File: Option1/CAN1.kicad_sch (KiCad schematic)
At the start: 7 parts, among them U2 TJA1051T-3

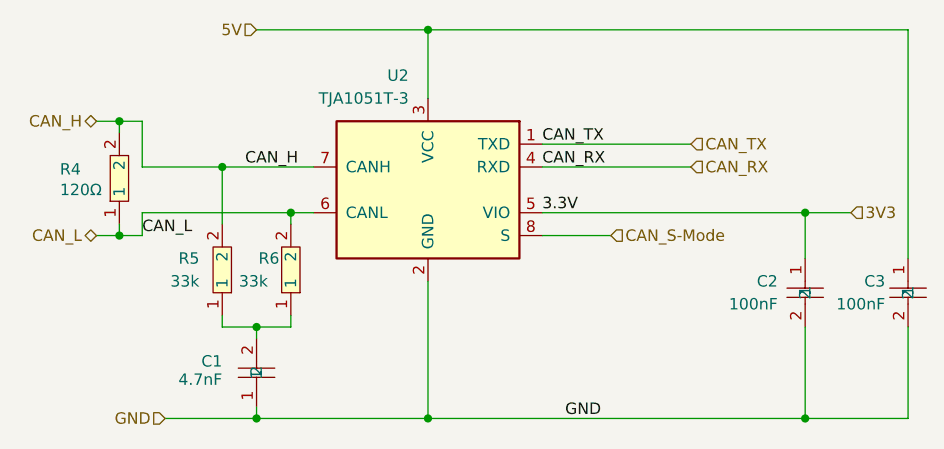
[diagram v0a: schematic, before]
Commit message: Layout für Powersupply, CAN und Stecker hinzugefügt
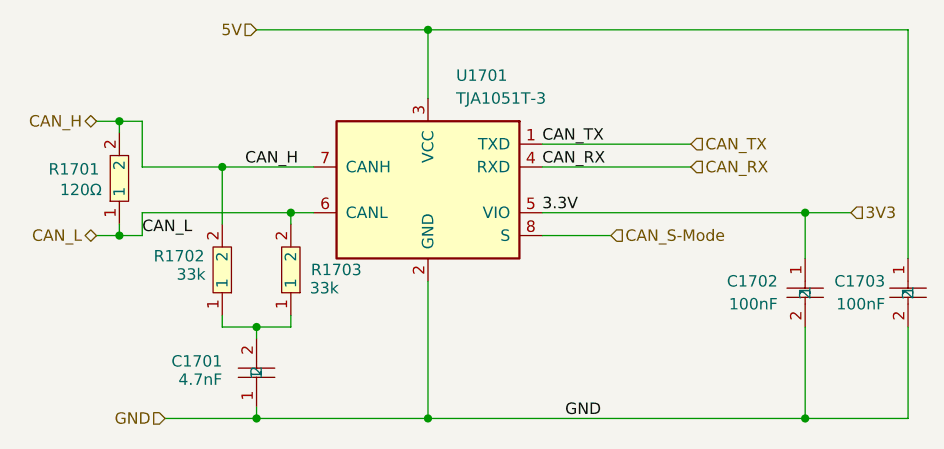
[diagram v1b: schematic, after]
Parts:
- renumbered C1 to C1701, C2 to C1702, C3 to C1703, R4 to R1701, R5 to R1702, R6 to R1703, U2 to U1701
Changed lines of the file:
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@@
 		(on_board yes)
 		(dnp no)
-		(property "Reference" "C2"
+		(property "Reference" "C1702"
 			(at 127.762 72.39 90)
 			(effects
@@
 			(project "Option1"
 				(path "/b9e5f262-9648-4b79-bdd1-af888b822329/5db2deb0-465f-47af-ae7a-0e9eee3d563c"
-					(reference "C2")
+					(reference "C1702")
 					(unit 1)
 				)
@@
 		(on_board yes)
 		(dnp no)
-		(fields_autoplaced yes)
-		(property "Reference" "R5"
-			(at 63.5 69.8499 90)
-			(effects
-				(font
-					(size 1.27 1.27)
-				)
-				(justify right)
+		(property "Reference" "R1702"
+			(at 58.42 69.596 90)
+			(effects
+				(font
+					(size 1.27 1.27)
+				)
+				(justify left)
 			)
 		)
 		(property "Value" "33k"
-			(at 63.5 72.3899 90)
-			(effects
-				(font
-					(size 1.27 1.27)
-				)
-				(justify right)
+			(at 60.96 71.628 90)
+			(effects
+				(font
+					(size 1.27 1.27)
+				)
+				(justify left)
 			)
 		)
@@
 			(project "Option1"
 				(path "/b9e5f262-9648-4b79-bdd1-af888b822329/5db2deb0-465f-47af-ae7a-0e9eee3d563c"
-					(reference "R5")
+					(reference "R1702")
 					(unit 1)
 				)
@@
 		(on_board yes)
 		(dnp no)
-		(property "Reference" "C3"
+		(property "Reference" "C1703"
 			(at 139.7 72.39 90)
 			(effects
@@
 			(project "Option1"
 				(path "/b9e5f262-9648-4b79-bdd1-af888b822329/5db2deb0-465f-47af-ae7a-0e9eee3d563c"
-					(reference "C3")
+					(reference "C1703")
 					(unit 1)
 				)
@@
 		(on_board yes)
 		(dnp no)
-		(property "Reference" "R4"
-			(at 48.006 59.944 90)
+		(property "Reference" "R1701"
+			(at 46.736 59.944 90)
 			(effects
 				(font
@@
 			(project "Option1"
 				(path "/b9e5f262-9648-4b79-bdd1-af888b822329/5db2deb0-465f-47af-ae7a-0e9eee3d563c"
-					(reference "R4")
+					(reference "R1701")
 					(unit 1)
 				)
@@
 		(dnp no)
 		(fields_autoplaced yes)
-		(property "Reference" "U2"
-			(at 86.7567 49.53 0)
-			(effects
-				(font
-					(size 1.27 1.27)
-				)
-				(justify left)
+		(property "Reference" "U1701"
+			(at 92.0181 49.53 0)
+			(effects
+				(font
+					(size 1.27 1.27)
+				)
+				(justify right)
 			)
 		)
 		(property "Value" "TJA1051T-3"
-			(at 86.7567 52.07 0)
-			(effects
-				(font
-					(size 1.27 1.27)
-				)
-				(justify left)
+			(at 92.0181 52.07 0)
+			(effects
+				(font
+					(size 1.27 1.27)
+				)
+				(justify right)
 			)
 		)
@@
 			(project "Option1"
 				(path "/b9e5f262-9648-4b79-bdd1-af888b822329/5db2deb0-465f-47af-ae7a-0e9eee3d563c"
-					(reference "U2")
+					(reference "U1701")
 					(unit 1)
 				)
@@
 		(on_board yes)
 		(dnp no)
-		(property "Reference" "C1"
+		(property "Reference" "C1701"
 			(at 66.04 81.2799 90)
 			(effects
@@
 			(project "Option1"
 				(path "/b9e5f262-9648-4b79-bdd1-af888b822329/5db2deb0-465f-47af-ae7a-0e9eee3d563c"
-					(reference "C1")
+					(reference "C1701")
 					(unit 1)
 				)
@@
 		(on_board yes)
 		(dnp no)
-		(property "Reference" "R6"
-			(at 72.39 69.85 90)
+		(property "Reference" "R1703"
+			(at 81.534 71.12 90)
 			(effects
 				(font
@@
 		)
 		(property "Value" "33k"
-			(at 71.12 72.3899 90)
+			(at 78.994 73.152 90)
 			(effects
 				(font
@@
 			(project "Option1"
 				(path "/b9e5f262-9648-4b79-bdd1-af888b822329/5db2deb0-465f-47af-ae7a-0e9eee3d563c"
-					(reference "R6")
-					(unit 1)
-				)
+					(reference "R1703")
+					(unit 1)
+				)

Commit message: GND polygon hinzugefügt, unverbundene Pads verknüpft, 0 Ohm Widerstand für Display Strohmversorgung hinzugefügt
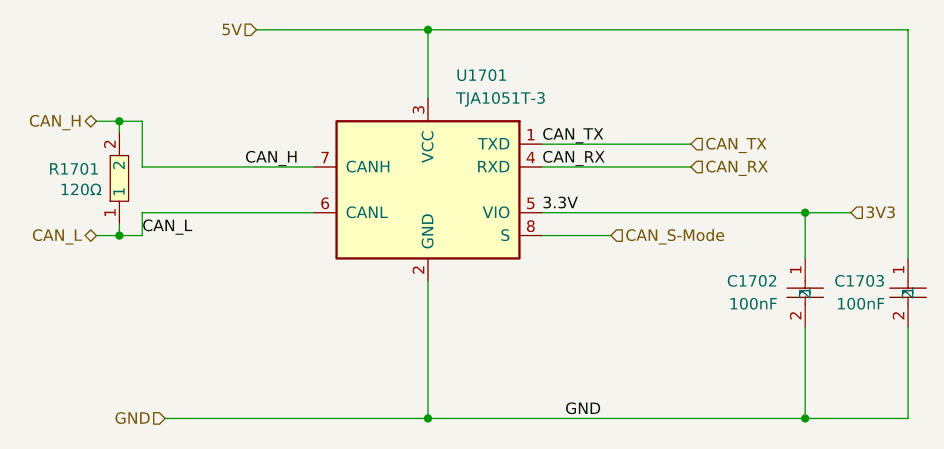
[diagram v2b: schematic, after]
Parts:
- removed C1701: 4.7nF, easyeda2kicad:C0805, symbol easyeda2kicad:0805B472K500NT
- removed R1702, R1703: 33k, easyeda2kicad:R0603, symbol easyeda2kicad:0603WAF3302T5E

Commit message: Schaltplan zu bachelorarbeit Dokument hinzuigefügt. Fertigf bis SPI Flash
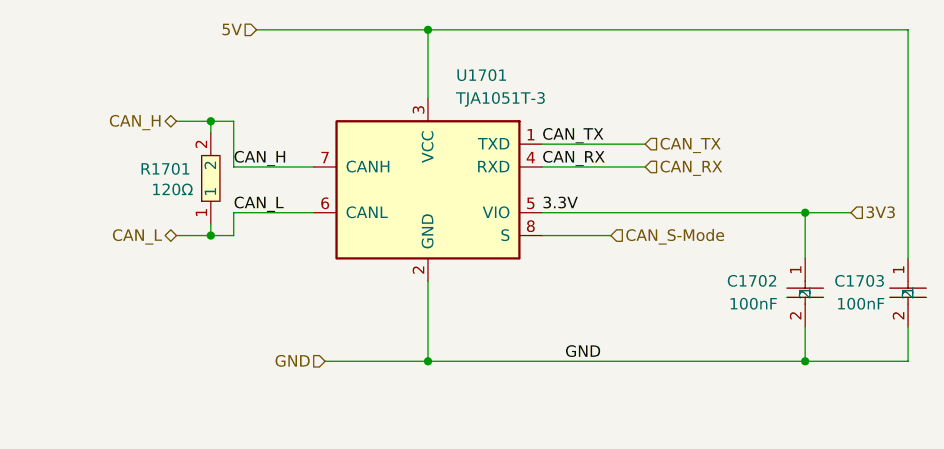
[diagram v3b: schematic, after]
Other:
- moved on the sheet: R1701
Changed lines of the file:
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@@
 	)
 	(junction
-		(at 54.61 67.31)
+		(at 130.81 81.28)
 		(diameter 0)
 		(color 0 0 0 0)
 	)
 	(junction
-		(at 54.61 54.61)
+		(at 64.77 67.31)
 		(diameter 0)
 		(color 0 0 0 0)
@@
 	)
 	(junction
-		(at 130.81 87.63)
+		(at 64.77 54.61)
+		(diameter 0)
+		(color 0 0 0 0)
+	)
+	(junction
+		(at 88.9 81.28)
 		(diameter 0)
 		(color 0 0 0 0)
@@
 		(color 0 0 0 0)
 	)
-	(junction
-		(at 88.9 87.63)
-		(diameter 0)
-		(color 0 0 0 0)
-	)
-	(wire
-		(pts
-			(xy 57.15 67.31) (xy 57.15 64.77)
+	(wire
+		(pts
+			(xy 64.77 67.31) (xy 67.31 67.31)
+		)
+		(stroke
+			(width 0)
+			(type default)
+		)
+	)
+	(wire
+		(pts
+			(xy 67.31 67.31) (xy 67.31 64.77)
 		)
 		(stroke
@@
 	(wire
 		(pts
-			(xy 142.24 87.63) (xy 130.81 87.63)
-		)
-		(stroke
-			(width 0)
-			(type default)
-		)
-	)
-	(wire
-		(pts
-			(xy 54.61 67.31) (xy 52.07 67.31)
-		)
-		(stroke
-			(width 0)
-			(type default)
-		)
-	)
-	(wire
-		(pts
-			(xy 57.15 54.61) (xy 57.15 59.69)
-		)
-		(stroke
-			(width 0)
-			(type default)
-		)
-	)
-	(wire
-		(pts
-			(xy 57.15 54.61) (xy 54.61 54.61)
-		)
-		(stroke
-			(width 0)
-			(type default)
-		)
-	)
-	(wire
-		(pts
-			(xy 57.15 64.77) (xy 76.2 64.77)
-		)
-		(stroke
-			(width 0)
-			(type default)
-		)
-	)
-	(wire
-		(pts
-			(xy 88.9 72.39) (xy 88.9 87.63)
-		)
-		(stroke
-			(width 0)
-			(type default)
-		)
-	)
-	(wire
-		(pts
-			(xy 130.81 77.47) (xy 130.81 87.63)
+			(xy 142.24 81.28) (xy 130.81 81.28)
+		)
+		(stroke
+			(width 0)
+			(type default)
+		)
+	)
+	(wire
+		(pts
+			(xy 60.96 67.31) (xy 64.77 67.31)
+		)
+		(stroke
+			(width 0)
+			(type default)
+		)
+	)
+	(wire
+		(pts
+			(xy 67.31 54.61) (xy 67.31 59.69)
+		)
+		(stroke
+			(width 0)
+			(type default)
+		)
+	)
+	(wire
+		(pts
+			(xy 67.31 54.61) (xy 64.77 54.61)
+		)
+		(stroke
+			(width 0)
+			(type default)
+		)
+	)
+	(wire
+		(pts
+			(xy 67.31 64.77) (xy 76.2 64.77)
+		)
+		(stroke
+			(width 0)
+			(type default)
+		)
+	)
+	(wire
+		(pts
+			(xy 88.9 72.39) (xy 88.9 81.28)
+		)
+		(stroke
+			(width 0)
+			(type default)
+		)
+	)
+	(wire
+		(pts
+			(xy 130.81 77.47) (xy 130.81 81.28)
 		)
 		(stroke
@@
 	(wire
 		(pts
-			(xy 57.15 67.31) (xy 54.61 67.31)
-		)
-		(stroke
-			(width 0)
-			(type default)
-		)
-	)
-	(wire
-		(pts
 			(xy 142.24 44.45) (xy 142.24 69.85)
 		)
@@
 	(wire
 		(pts
-			(xy 54.61 54.61) (xy 54.61 55.88)
-		)
-		(stroke
-			(width 0)
-			(type default)
-		)
-	)
-	(wire
-		(pts
-			(xy 101.6 59.69) (xy 118.11 59.69)
-		)
-		(stroke
-			(width 0)
-			(type default)
-		)
-	)
-	(wire
-		(pts
-			(xy 101.6 57.15) (xy 118.11 57.15)
-		)
-		(stroke
-			(width 0)
-			(type default)
-		)
-	)
-	(wire
-		(pts
-			(xy 59.69 87.63) (xy 88.9 87.63)
+			(xy 64.77 54.61) (xy 64.77 55.88)
+		)
+		(stroke
+			(width 0)
+			(type default)
+		)
+	)
+	(wire
+		(pts
+			(xy 101.6 59.69) (xy 113.03 59.69)
+		)
+		(stroke
+			(width 0)
+			(type default)
+		)
+	)
+	(wire
+		(pts
+			(xy 101.6 57.15) (xy 113.03 57.15)
+		)
+		(stroke
+			(width 0)
+			(type default)
+		)
+	)
+	(wire
+		(pts
+			(xy 77.47 81.28) (xy 88.9 81.28)
 		)
 		(stroke
@@
 	(wire
 		(pts
-			(xy 57.15 59.69) (xy 76.2 59.69)
-		)
-		(stroke
-			(width 0)
-			(type default)
-		)
-	)
-	(wire
-		(pts
-			(xy 130.81 87.63) (xy 88.9 87.63)
-		)
-		(stroke
-			(width 0)
-			(type default)
-		)
-	)
-	(wire
-		(pts
-			(xy 54.61 66.04) (xy 54.61 67.31)
-		)
-		(stroke
-			(width 0)
-			(type default)
-		)
-	)
-	(wire
-		(pts
-			(xy 142.24 77.47) (xy 142.24 87.63)
+			(xy 67.31 59.69) (xy 76.2 59.69)
+		)
+		(stroke
+			(width 0)
+			(type default)
+		)
+	)
+	(wire
+		(pts
+			(xy 130.81 81.28) (xy 88.9 81.28)
+		)
+		(stroke
+			(width 0)
+			(type default)
+		)
+	)
+	(wire
+		(pts
+			(xy 64.77 66.04) (xy 64.77 67.31)
+		)
+		(stroke
+			(width 0)
+			(type default)
+		)
+	)
+	(wire
+		(pts
+			(xy 142.24 77.47) (xy 142.24 81.28)
 		)
 		(stroke
@@
 	(wire
 		(pts
-			(xy 54.61 54.61) (xy 52.07 54.61)
+			(xy 60.96 54.61) (xy 64.77 54.61)
 		)
 		(stroke
@@
 	)
 	(label "GND"
-		(at 104.14 87.63 0)
+		(at 104.14 81.28 0)
 		(effects
 			(font
@@
 	)
 	(label "CAN_L"
-		(at 57.15 67.31 0)
+		(at 67.31 64.77 0)
 		(effects
 			(font
@@
 	)
 	(label "CAN_H"
-		(at 68.58 59.69 0)
+		(at 67.31 59.69 0)
 		(effects
 			(font
@@
 	(hierarchical_label "CAN_L"
 		(shape bidirectional)
-		(at 52.07 67.31 180)
+		(at 60.96 67.31 180)
 		(effects
 			(font
@@
 	(hierarchical_label "CAN_TX"
 		(shape input)
-		(at 118.11 57.15 0)
+		(at 113.03 57.15 0)
 		(effects
 			(font
@@
 	(hierarchical_label "GND"
 		(shape input)
-		(at 59.69 87.63 180)
+		(at 77.47 81.28 180)
 		(effects
 			(font
@@
 	(hierarchical_label "CAN_H"
 		(shape bidirectional)
-		(at 52.07 54.61 180)
+		(at 60.96 54.61 180)
 		(effects
 			(font
@@
 	(hierarchical_label "CAN_RX"
 		(shape input)
-		(at 118.11 59.69 0)
+		(at 113.03 59.69 0)
 		(effects
 			(font
@@
 	(symbol
 		(lib_id "EasyEda2KiCad:0603WAF1200T5E")
-		(at 54.61 60.96 90)
+		(at 64.77 60.96 90)
 		(unit 1)
 		(exclude_from_sim no)
@@
 		(dnp no)
 		(property "Reference" "R1701"
-			(at 46.736 59.944 90)
+			(at 56.896 59.944 90)
 			(effects
 				(font
@@
 		)
 		(property "Value" "120Ω"
-			(at 48.006 62.23 90)
+			(at 58.166 62.23 90)
 			(effects
 				(font
@@
 		)
 		(property "Footprint" "easyeda2kicad:R0603"
-			(at 62.23 60.96 0)
+			(at 72.39 60.96 0)
 			(effects
 				(font
@@
 		)
 		(property "Datasheet" "https://lcsc.com/product-detail/Chip-Resistor-Surface-Mount-UniOhm_120R-1200-1_C22787.html"
+			(at 74.93 60.96 0)
+			(effects
+				(font
+					(size 1.27 1.27)
+				)
+				(hide yes)
+			)
+		)
+		(property "Description" ""
 			(at 64.77 60.96 0)
 			(effects
@@
 			)
 		)
-		(property "Description" ""
-			(at 54.61 60.96 0)
-			(effects
-				(font
-					(size 1.27 1.27)
-				)
-				(hide yes)
-			)
-		)
 		(property "LCSC Part" "C22787"
-			(at 67.31 60.96 0)
-			(effects
-				(font
+			(at 77.47 60.96 0)
+			(effects
+				(font
